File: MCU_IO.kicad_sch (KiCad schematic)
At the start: 27 parts, among them J1 Conn_02x07_Odd_Even, J10 Conn_01x05, U7 TMS320F28379DPTPQ, U8 M24512, U9 MAX809, Y1 10 MHz

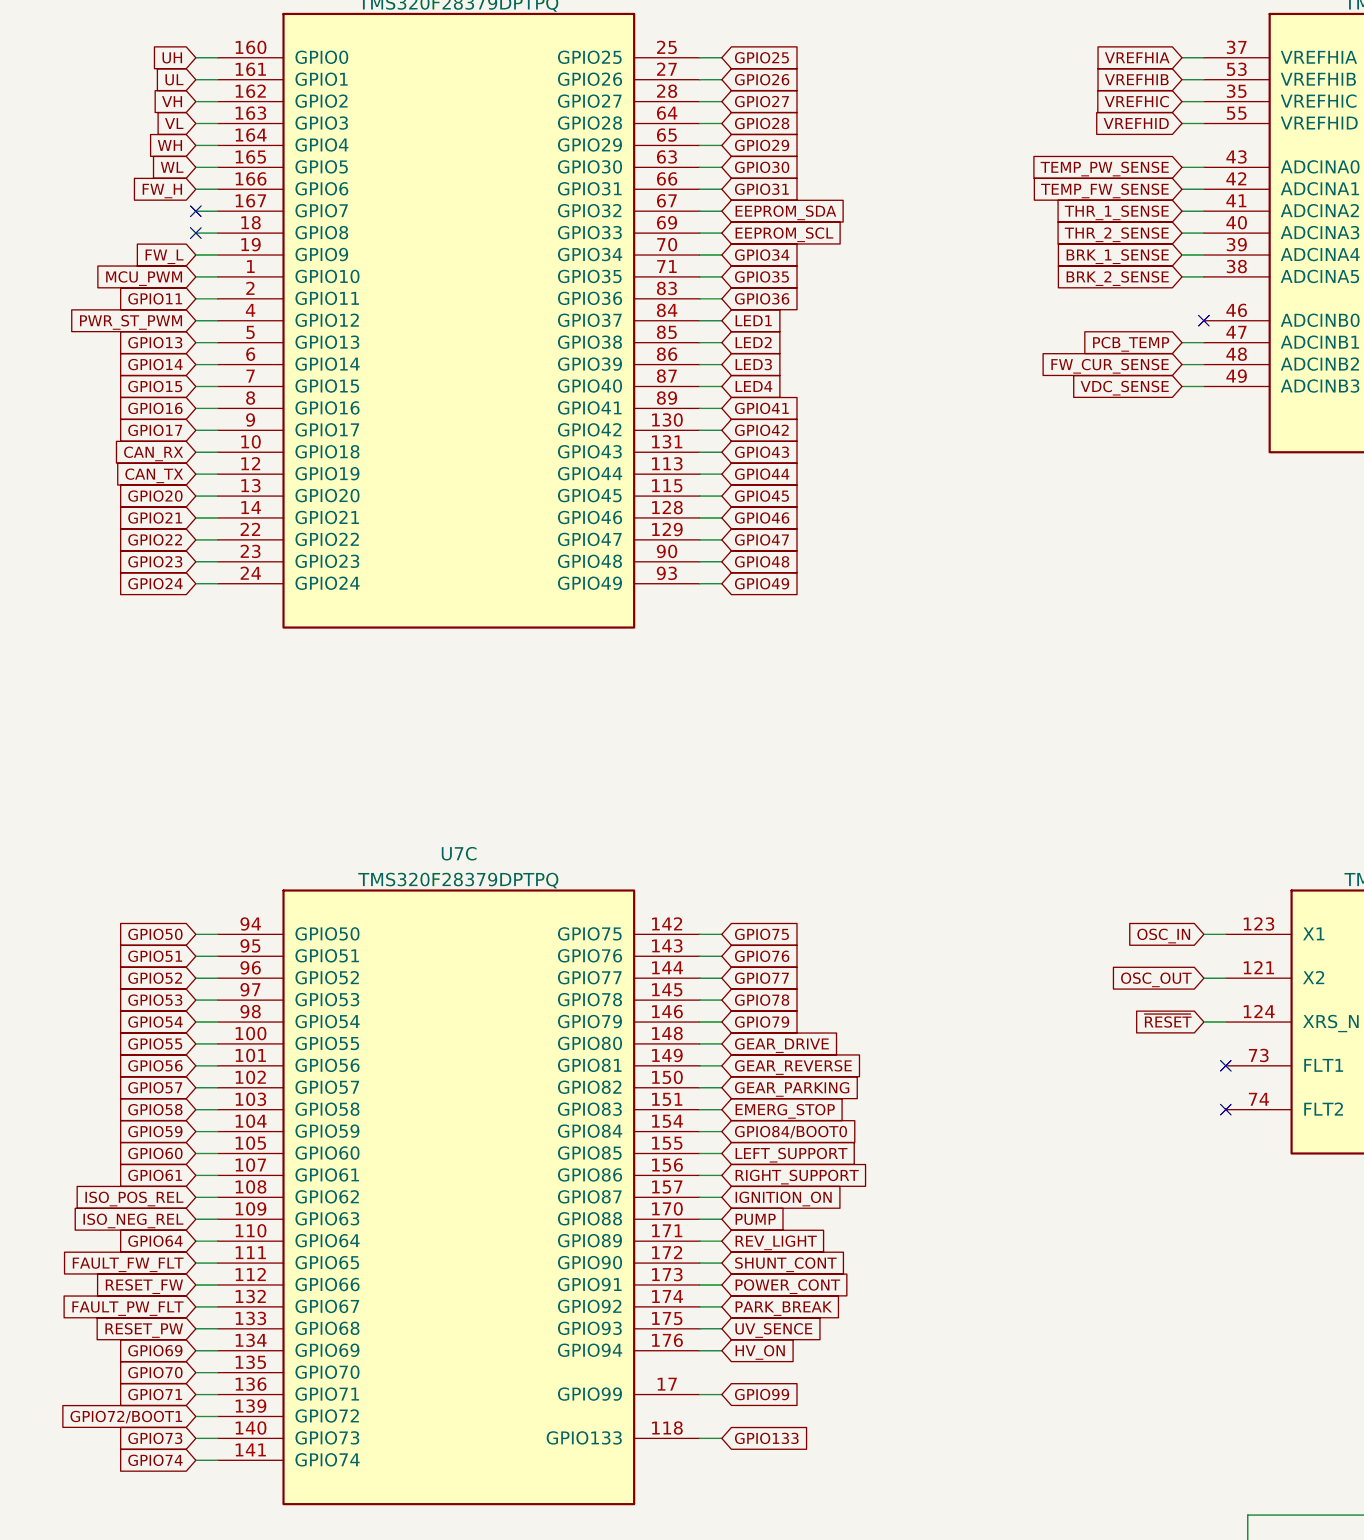
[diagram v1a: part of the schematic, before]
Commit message: Исправление: в схеме добавил обработку температур, изменил обработку токов
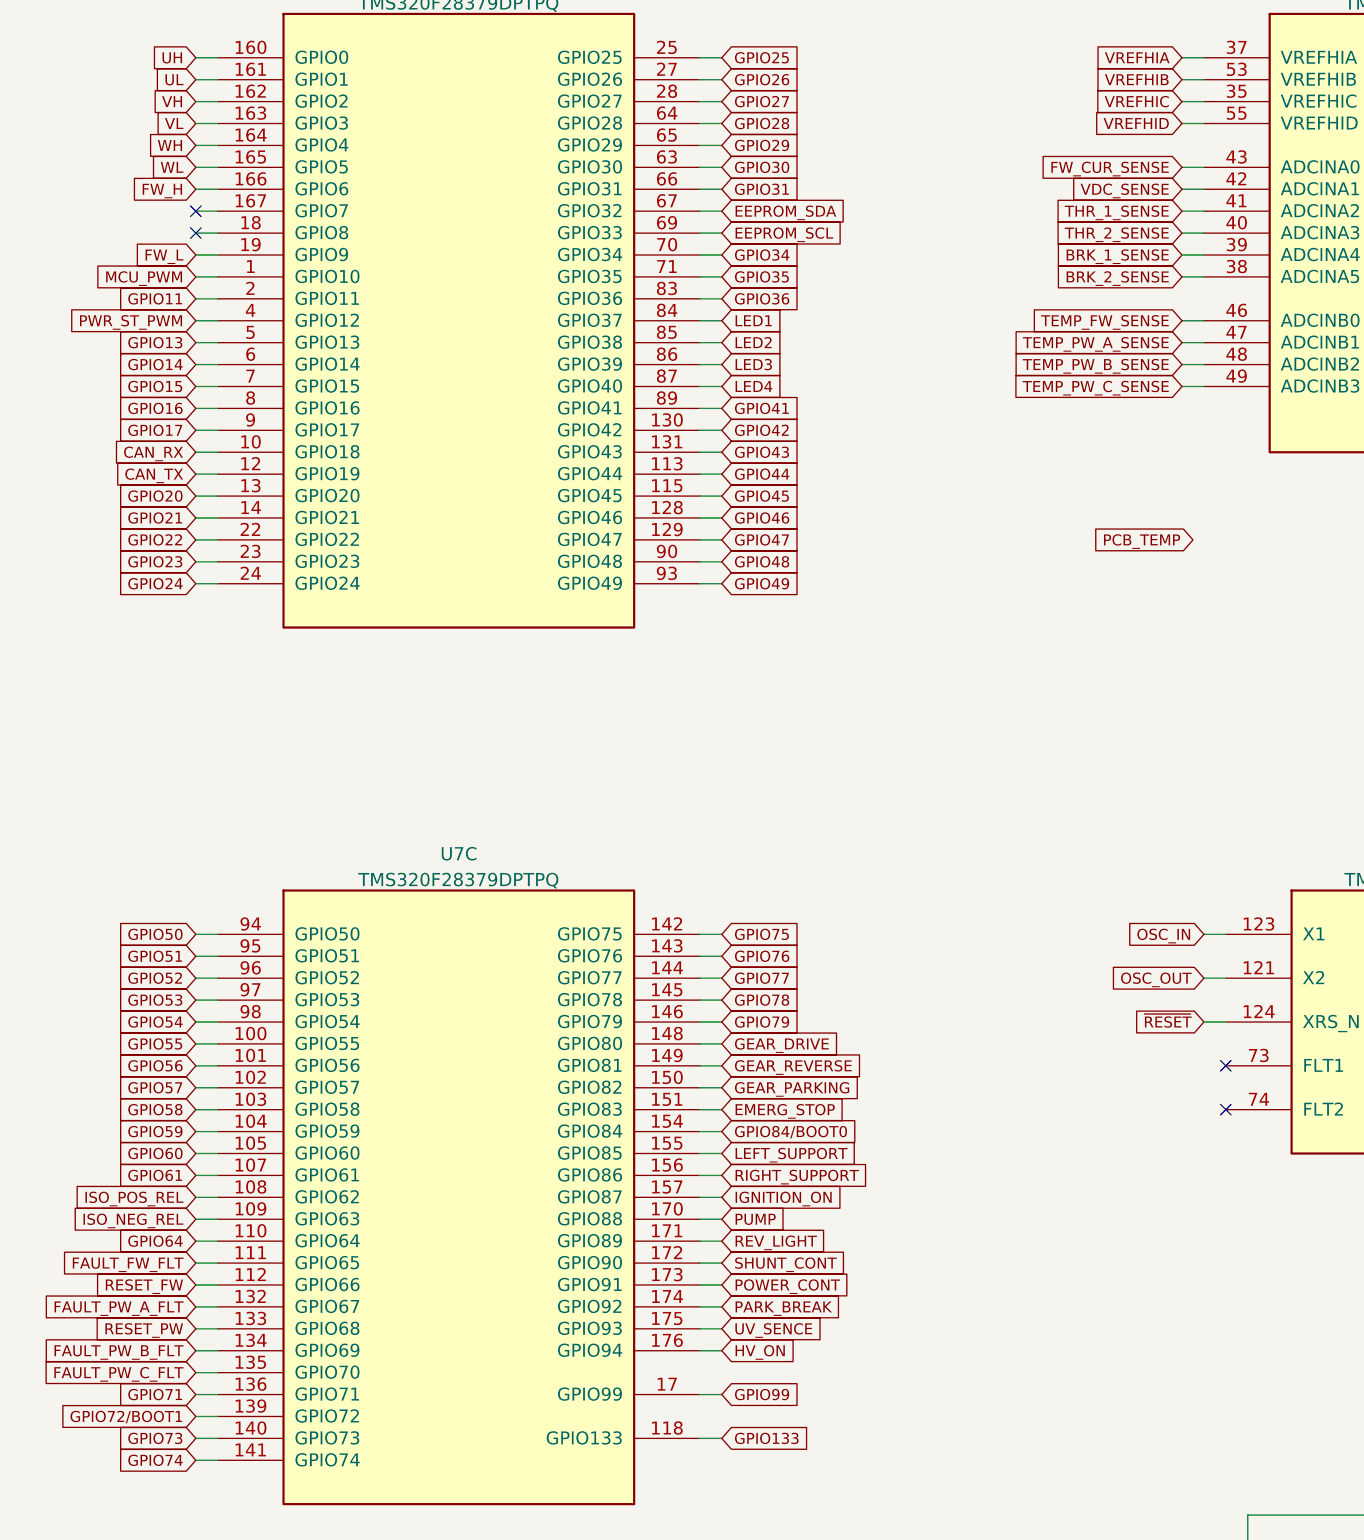
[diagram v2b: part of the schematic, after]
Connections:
- net TEMP_PW_SENSE is gone; now on net FW_CUR_SENSE: U7.43 (ADCINA0)
- net FW_CUR_SENSE: no longer U7.48 (ADCINB2)
- net PCB_TEMP: no longer U7.47 (ADCINB1)
- net TEMP_FW_SENSE: now also U7.46 (ADCINB0); no longer U7.42 (ADCINA1)
- net VDC_SENSE: now also U7.42 (ADCINA1); no longer U7.49 (ADCINB3)
- net FAULT_PW_FLT renamed FAULT_PW_A_FLT
- net GPIO69 renamed FAULT_PW_B_FLT
- net GPIO70 renamed FAULT_PW_C_FLT
- new net TEMP_PW_A_SENSE: U7.47 (ADCINB1)
- new net TEMP_PW_B_SENSE: U7.48 (ADCINB2)
- new net TEMP_PW_C_SENSE: U7.49 (ADCINB3)
- no-connect marks 11 -> 10
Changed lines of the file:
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@@
 		(at 341.63 60.96)
 	)
-	(no_connect
-		(at 181.61 73.66)
-	)
 	(wire
 		(pts
@@
 	(wire
 		(pts
+			(xy 179.07 73.66) (xy 181.61 73.66)
+		)
+		(stroke
+			(width 0)
+			(type default)
+		)
+	)
+	(wire
+		(pts
 			(xy 344.17 73.66) (xy 344.17 71.12)
 		)
@@
 		)
 	)
+	(global_label "TEMP_PW_B_SENSE"
+		(shape input)
+		(at 179.07 78.74 180)
+		(fields_autoplaced yes)
+		(effects
+			(font
+				(size 1.27 1.27)
+			)
+			(justify right)
+		)
+		(property "Intersheetrefs" "${INTERSHEET_REFS}"
+			(at 158.3051 78.74 0)
+			(effects
+				(font
+					(size 1.27 1.27)
+				)
+				(justify right)
+				(hide yes)
+			)
+		)
+	)
 	(global_label "GPIO42"
 		(shape input)
@@
 		)
 	)
-	(global_label "FAULT_PW_FLT"
-		(shape input)
-		(at 64.77 187.96 180)
-		(fields_autoplaced yes)
-		(effects
-			(font
-				(size 1.27 1.27)
-			)
-			(justify right)
-		)
-		(property "Intersheetrefs" "${INTERSHEET_REFS}"
-			(at 49.1126 187.8806 0)
-			(effects
-				(font
-					(size 1.27 1.27)
-				)
-				(justify right)
-				(hide yes)
-			)
-		)
-	)
 	(global_label "GPIO29"
 		(shape input)
@@
 	(global_label "TEMP_FW_SENSE"
 		(shape input)
-		(at 179.07 58.42 180)
+		(at 179.07 73.66 180)
 		(fields_autoplaced yes)
 		(effects
@@
 		)
 		(property "Intersheetrefs" "${INTERSHEET_REFS}"
-			(at 161.2959 58.4994 0)
+			(at 161.2959 73.7394 0)
 			(effects
 				(font
@@
 	(global_label "VDC_SENSE"
 		(shape input)
-		(at 179.07 81.28 180)
+		(at 179.07 58.42 180)
 		(fields_autoplaced yes)
 		(effects
@@
 		)
 		(property "Intersheetrefs" "${INTERSHEET_REFS}"
-			(at 166.0131 81.3594 0)
+			(at 166.0131 58.4994 0)
 			(effects
 				(font
@@
 		)
 	)
-	(global_label "GPIO70"
-		(shape input)
-		(at 64.77 195.58 180)
-		(fields_autoplaced yes)
-		(effects
-			(font
-				(size 1.27 1.27)
-			)
-			(justify right)
-		)
-		(property "Intersheetrefs" "${INTERSHEET_REFS}"
-			(at 55.4626 195.5006 0)
-			(effects
-				(font
-					(size 1.27 1.27)
-				)
-				(justify right)
-				(hide yes)
-			)
-		)
-	)
 	(global_label "GPIO21"
 		(shape input)
@@
 		)
 	)
+	(global_label "FAULT_PW_A_FLT"
+		(shape input)
+		(at 64.77 187.96 180)
+		(fields_autoplaced yes)
+		(effects
+			(font
+				(size 1.27 1.27)
+			)
+			(justify right)
+		)
+		(property "Intersheetrefs" "${INTERSHEET_REFS}"
+			(at 46.4843 187.96 0)
+			(effects
+				(font
+					(size 1.27 1.27)
+				)
+				(justify right)
+				(hide yes)
+			)
+		)
+	)
 	(global_label "GPIO75"
 		(shape input)
@@
 	(global_label "FW_CUR_SENSE"
 		(shape input)
-		(at 179.07 78.74 180)
+		(at 179.07 55.88 180)
 		(fields_autoplaced yes)
 		(effects
@@
 		)
 		(property "Intersheetrefs" "${INTERSHEET_REFS}"
-			(at 162.2636 78.6606 0)
+			(at 162.2636 55.8006 0)
 			(effects
 				(font
@@
 		)
 	)
-	(global_label "PCB_TEMP"
-		(shape input)
-		(at 179.07 76.2 180)
-		(fields_autoplaced yes)
-		(effects
-			(font
-				(size 1.27 1.27)
-			)
-			(justify right)
-		)
-		(property "Intersheetrefs" "${INTERSHEET_REFS}"
-			(at 280.67 243.84 0)
-			(effects
-				(font
-					(size 1.27 1.27)
-				)
-				(hide yes)
-			)
-		)
-	)
-	(global_label "GPIO69"
-		(shape input)
-		(at 64.77 193.04 180)
-		(fields_autoplaced yes)
-		(effects
-			(font
-				(size 1.27 1.27)
-			)
-			(justify right)
-		)
-		(property "Intersheetrefs" "${INTERSHEET_REFS}"
-			(at 55.4626 192.9606 0)
-			(effects
-				(font
-					(size 1.27 1.27)
-				)
-				(justify right)
-				(hide yes)
-			)
-		)
-	)
 	(global_label "GPIO20"
 		(shape input)
@@
 		)
 	)
+	(global_label "FAULT_PW_C_FLT"
+		(shape input)
+		(at 64.77 195.58 180)
+		(fields_autoplaced yes)
+		(effects
+			(font
+				(size 1.27 1.27)
+			)
+			(justify right)
+		)
+		(property "Intersheetrefs" "${INTERSHEET_REFS}"
+			(at 46.3029 195.58 0)
+			(effects
+				(font
+					(size 1.27 1.27)
+				)
+				(justify right)
+				(hide yes)
+			)
+		)
+	)
 	(global_label "VREFHIC"
 		(shape input)
@@
 		)
 	)
+	(global_label "FAULT_PW_B_FLT"
+		(shape input)
+		(at 64.77 193.04 180)
+		(fields_autoplaced yes)
+		(effects
+			(font
+				(size 1.27 1.27)
+			)
+			(justify right)
+		)
+		(property "Intersheetrefs" "${INTERSHEET_REFS}"
+			(at 46.3029 193.04 0)
+			(effects
+				(font
+					(size 1.27 1.27)
+				)
+				(justify right)
+				(hide yes)
+			)
+		)
+	)
 	(global_label "GPIO28"
 		(shape input)
@@
 		)
 	)
-	(global_label "GPIO17"
+	(global_label "TEMP_PW_C_SENSE"
 		(shape input)
-		(at 64.77 86.36 180)
+		(at 179.07 81.28 180)
 		(fields_autoplaced yes)
 		(effects
@@
 		)
 		(property "Intersheetrefs" "${INTERSHEET_REFS}"
-			(at 56.6721 86.2806 0)
+			(at 158.3051 81.28 0)
 			(effects
 				(font
@@
 		)
 	)
-	(global_label "UV_SENCE"
+	(global_label "TEMP_PW_A_SENSE"
 		(shape input)
-		(at 125.73 190.5 0)
+		(at 179.07 76.2 180)
 		(fields_autoplaced yes)
 		(effects
@@
 				(size 1.27 1.27)
 			)
-			(justify left)
+			(justify right)
 		)
 		(property "Intersheetrefs" "${INTERSHEET_REFS}"
-			(at 137.6379 190.4206 0)
+			(at 158.4865 76.2 0)
 			(effects
 				(font
 					(size 1.27 1.27)
 				)
-				(justify left)
+				(justify right)
 				(hide yes)
 			)
 		)
 	)
-	(global_label "TEMP_PW_SENSE"
+	(global_label "PCB_TEMP"
 		(shape input)
-		(at 179.07 55.88 180)
+		(at 180.34 99.06 180)
 		(fields_autoplaced yes)
 		(effects
@@
 		)
 		(property "Intersheetrefs" "${INTERSHEET_REFS}"
-			(at 161.1145 55.9594 0)
+			(at 167.7392 99.06 0)
 			(effects
 				(font
@@
 				(hide yes)
 			)
+		)
+	)
+	(global_label "GPIO17"
+		(shape input)
+		(at 64.77 86.36 180)
+		(fields_autoplaced yes)
+		(effects
+			(font
+				(size 1.27 1.27)
+			)
+			(justify right)
+		)
+		(property "Intersheetrefs" "${INTERSHEET_REFS}"
+			(at 56.6721 86.2806 0)
+			(effects
+				(font
+					(size 1.27 1.27)
+				)
+				(justify right)
+				(hide yes)
+			)
+		)
+	)
+	(global_label "UV_SENCE"
+		(shape input)
+		(at 125.73 190.5 0)
+		(fields_autoplaced yes)
+		(effects
+			(font
+				(size 1.27 1.27)
+			)
+			(justify left)
+		)
+		(property "Intersheetrefs" "${INTERSHEET_REFS}"
+			(at 137.6379 190.4206 0)
+			(effects
+				(font
+					(size 1.27 1.27)
+				)
+				(justify left)
+				(hide yes)
+			)

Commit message: Добавления: Расставил все на плате
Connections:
- net TEMP_PW_A_SENSE is gone; now on net PCB_TEMP: U7.47 (ADCINB1)
- net TEMP_PW_B_SENSE is gone; now on net FW_CUR_SENSE: U7.48 (ADCINB2)
- net TEMP_PW_C_SENSE is gone; now on net VDC_SENSE: U7.49 (ADCINB3)
- net FW_CUR_SENSE: no longer U7.43 (ADCINA0)
- net TEMP_FW_SENSE: now also U7.42 (ADCINA1); no longer U7.46 (ADCINB0)
- net VDC_SENSE: no longer U7.42 (ADCINA1)
- new net TEMP_PW_SENSE: U7.43 (ADCINA0)
- no-connect marks 10 -> 11
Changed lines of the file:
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@@
 	)
 	(no_connect
+		(at 179.07 73.66)
+	)
+	(no_connect
 		(at 198.12 224.79)
 	)
@@
 		)
 	)
-	(global_label "TEMP_PW_B_SENSE"
+	(global_label "GPIO42"
 		(shape input)
-		(at 179.07 78.74 180)
+		(at 125.73 86.36 0)
 		(fields_autoplaced yes)
 		(effects
@@
 				(size 1.27 1.27)
 			)
-			(justify right)
+			(justify left)
 		)
 		(property "Intersheetrefs" "${INTERSHEET_REFS}"
-			(at 158.3051 78.74 0)
+			(at 135.0374 86.2806 0)
 			(effects
 				(font
 					(size 1.27 1.27)
 				)
-				(justify right)
+				(justify left)
 				(hide yes)
 			)
 		)
 	)
-	(global_label "GPIO42"
+	(global_label "S0_TEMP_MULIPLEX"
 		(shape input)
-		(at 125.73 86.36 0)
+		(at 274.32 113.03 180)
 		(fields_autoplaced yes)
 		(effects
@@
 				(size 1.27 1.27)
 			)
-			(justify left)
+			(justify right)
 		)
 		(property "Intersheetrefs" "${INTERSHEET_REFS}"
-			(at 135.0374 86.2806 0)
+			(at 253.0712 113.03 0)
 			(effects
 				(font
 					(size 1.27 1.27)
 				)
-				(justify left)
+				(justify right)
 				(hide yes)
 			)
@@
 	(global_label "TEMP_FW_SENSE"
 		(shape input)
-		(at 179.07 73.66 180)
+		(at 179.07 58.42 180)
 		(fields_autoplaced yes)
 		(effects
@@
 		)
 		(property "Intersheetrefs" "${INTERSHEET_REFS}"
-			(at 161.2959 73.7394 0)
+			(at 161.2959 58.4994 0)
 			(effects
 				(font
@@
 	(global_label "VDC_SENSE"
 		(shape input)
-		(at 179.07 58.42 180)
+		(at 179.07 81.28 180)
 		(fields_autoplaced yes)
 		(effects
@@
 		)
 		(property "Intersheetrefs" "${INTERSHEET_REFS}"
-			(at 166.0131 58.4994 0)
+			(at 166.0131 81.3594 0)
 			(effects
 				(font
@@
 	(global_label "FW_CUR_SENSE"
 		(shape input)
-		(at 179.07 55.88 180)
+		(at 179.07 78.74 180)
 		(fields_autoplaced yes)
 		(effects
@@
 		)
 		(property "Intersheetrefs" "${INTERSHEET_REFS}"
-			(at 162.2636 55.8006 0)
+			(at 162.2636 78.6606 0)
 			(effects
 				(font
@@
 		)
 	)
-	(global_label "OSC_OUT"
+	(global_label "S1_TEMP_MULIPLEX"
 		(shape input)
-		(at 181.61 149.86 180)
+		(at 274.32 115.57 180)
 		(fields_autoplaced yes)
 		(effects
@@
 		)
 		(property "Intersheetrefs" "${INTERSHEET_REFS}"
-			(at 170.7907 149.7806 0)
+			(at 253.0712 115.57 0)
 			(effects
 				(font
@@
 		)
 	)
-	(global_label "TEMP_PW_C_SENSE"
+	(global_label "OSC_OUT"
 		(shape input)
-		(at 179.07 81.28 180)
+		(at 181.61 149.86 180)
 		(fields_autoplaced yes)
 		(effects
@@
 		)
 		(property "Intersheetrefs" "${INTERSHEET_REFS}"
-			(at 158.3051 81.28 0)
+			(at 170.7907 149.7806 0)
 			(effects
 				(font
@@
 		)
 	)
-	(global_label "TEMP_PW_A_SENSE"
+	(global_label "TEMP_PW_SENSE"
 		(shape input)
-		(at 179.07 76.2 180)
+		(at 179.07 55.88 180)
 		(fields_autoplaced yes)
 		(effects
@@
 		)
 		(property "Intersheetrefs" "${INTERSHEET_REFS}"
-			(at 158.4865 76.2 0)
+			(at 160.5427 55.88 0)
 			(effects
 				(font
@@
 	(global_label "PCB_TEMP"
 		(shape input)
-		(at 180.34 99.06 180)
+		(at 179.07 76.2 180)
 		(fields_autoplaced yes)
 		(effects
@@
 		)
 		(property "Intersheetrefs" "${INTERSHEET_REFS}"
-			(at 167.7392 99.06 0)
+			(at 166.4692 76.2 0)
 			(effects
 				(font
@@
 				(hide yes)
 			)
+		)
+	)
+	(global_label "S2_TEMP_MULIPLEX"
+		(shape input)
+		(at 274.32 118.11 180)
+		(fields_autoplaced yes)
+		(effects
+			(font
+				(size 1.27 1.27)
+			)
+			(justify right)
+		)
+		(property "Intersheetrefs" "${INTERSHEET_REFS}"
+			(at 253.0712 118.11 0)
+			(effects
+				(font
+					(size 1.27 1.27)
+				)
+				(justify right)
+				(hide yes)
+			)

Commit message: Изменения: развел все
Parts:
- R223, R224, R225, R226: value 1.5k -> 680
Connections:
- net GPIO13 is gone; now on net S0_TEMP_MULIPLEX: U7.5 (GPIO13)
- net GPIO14 is gone; now on net S1_TEMP_MULIPLEX: U7.6 (GPIO14)
- net GPIO15 is gone; now on net S2_TEMP_MULIPLEX: U7.7 (GPIO15)
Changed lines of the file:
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@@
 	(global_label "S0_TEMP_MULIPLEX"
 		(shape input)
-		(at 274.32 113.03 180)
+		(at 64.77 76.2 180)
 		(fields_autoplaced yes)
 		(effects
@@
 		)
 		(property "Intersheetrefs" "${INTERSHEET_REFS}"
-			(at 253.0712 113.03 0)
+			(at 43.5212 76.2 0)
 			(effects
 				(font
@@
 		)
 	)
-	(global_label "GPIO14"
-		(shape input)
-		(at 64.77 78.74 180)
-		(fields_autoplaced yes)
-		(effects
-			(font
-				(size 1.27 1.27)
-			)
-			(justify right)
-		)
-		(property "Intersheetrefs" "${INTERSHEET_REFS}"
-			(at 56.6721 78.6606 0)
-			(effects
-				(font
-					(size 1.27 1.27)
-				)
-				(justify right)
-				(hide yes)
-			)
-		)
-	)
 	(global_label "GPIO53"
 		(shape input)
@@
 		)
 	)
-	(global_label "GPIO15"
-		(shape input)
-		(at 64.77 81.28 180)
-		(fields_autoplaced yes)
-		(effects
-			(font
-				(size 1.27 1.27)
-			)
-			(justify right)
-		)
-		(property "Intersheetrefs" "${INTERSHEET_REFS}"
-			(at 56.6721 81.2006 0)
-			(effects
-				(font
-					(size 1.27 1.27)
-				)
-				(justify right)
-				(hide yes)
-			)
-		)
-	)
 	(global_label "REV_LIGHT"
 		(shape input)
@@
 	(global_label "S1_TEMP_MULIPLEX"
 		(shape input)
-		(at 274.32 115.57 180)
+		(at 64.77 78.74 180)
 		(fields_autoplaced yes)
 		(effects
@@
 		)
 		(property "Intersheetrefs" "${INTERSHEET_REFS}"
-			(at 253.0712 115.57 0)
+			(at 43.5212 78.74 0)
 			(effects
 				(font
@@
 		)
 	)
-	(global_label "GPIO13"
-		(shape input)
-		(at 64.77 76.2 180)
-		(fields_autoplaced yes)
-		(effects
-			(font
-				(size 1.27 1.27)
-			)
-			(justify right)
-		)
-		(property "Intersheetrefs" "${INTERSHEET_REFS}"
-			(at 56.6721 76.1206 0)
-			(effects
-				(font
-					(size 1.27 1.27)
-				)
-				(justify right)
-				(hide yes)
-			)
-		)
-	)
 	(global_label "AW_TEMP_SENSE"
 		(shape input)
@@
 	(global_label "S2_TEMP_MULIPLEX"
 		(shape input)
-		(at 274.32 118.11 180)
+		(at 64.77 81.28 180)
 		(fields_autoplaced yes)
 		(effects
@@
 		)
 		(property "Intersheetrefs" "${INTERSHEET_REFS}"
-			(at 253.0712 118.11 0)
+			(at 43.5212 81.28 0)
 			(effects
 				(font
@@
 		(on_board yes)
 		(dnp no)
-		(fields_autoplaced yes)
 		(property "Reference" "R224"
-			(at 105.41 242.9342 90)
+			(at 105.41 242.57 90)
 			(effects
 				(font
@@
 			)
 		)
-		(property "Value" "1.5k"
-			(at 105.41 245.4711 90)
+		(property "Value" "680"
+			(at 105.41 245.11 90)
 			(effects
 				(font
@@
 		(on_board yes)
 		(dnp no)
-		(fields_autoplaced yes)
 		(property "Reference" "R225"
-			(at 105.41 255.6342 90)
+			(at 105.41 255.27 90)
 			(effects
 				(font
@@
 			)
 		)
-		(property "Value" "1.5k"
-			(at 105.41 258.1711 90)
+		(property "Value" "680"
+			(at 105.41 257.81 90)
 			(effects
 				(font
@@
 		(on_board yes)
 		(dnp no)
-		(fields_autoplaced yes)
 		(property "Reference" "R223"
-			(at 105.41 230.2342 90)
+			(at 105.41 229.87 90)
 			(effects
 				(font
@@
 			)
 		)
-		(property "Value" "1.5k"
-			(at 105.41 232.7711 90)
+		(property "Value" "680"
+			(at 105.41 232.41 90)
 			(effects
 				(font
@@
 			)
 		)
-		(property "Value" "1.5k"
+		(property "Value" "680"
 			(at 105.41 270.8711 90)
 			(effects
